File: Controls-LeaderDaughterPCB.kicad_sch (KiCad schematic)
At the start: 30 parts, among them U8 LMC555xM

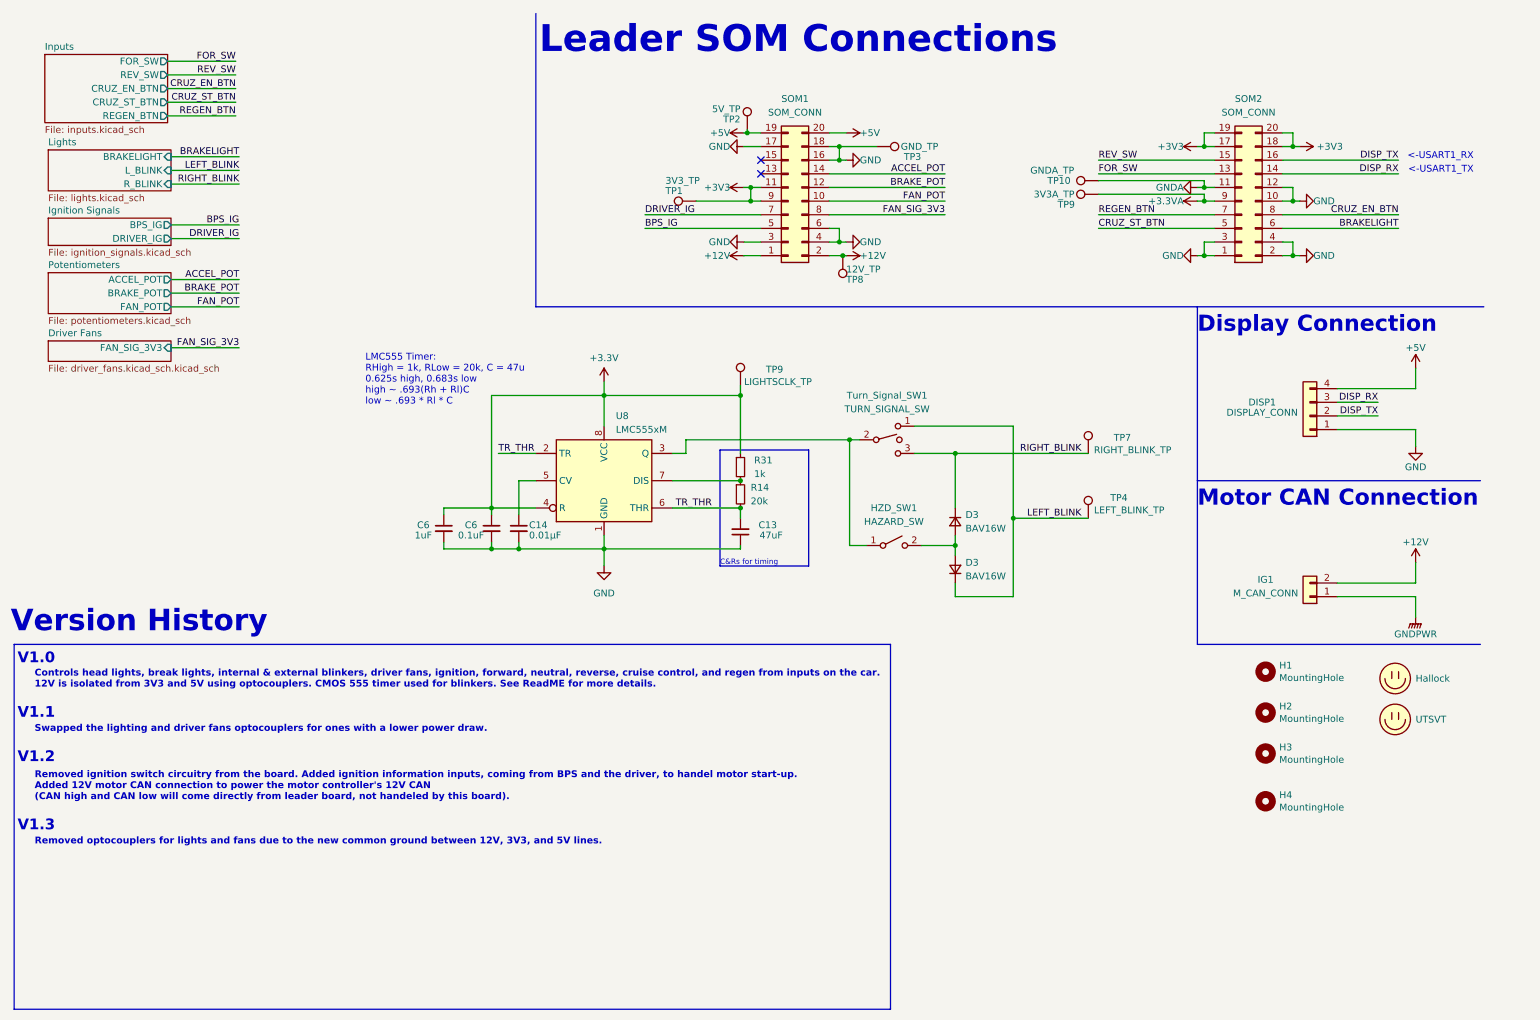
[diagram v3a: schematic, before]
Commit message: Added I2C GPIO expander to reduce GPIO pins from LeaderSOM and replace 555 timer circuit. Adjusted ignition switch signals.
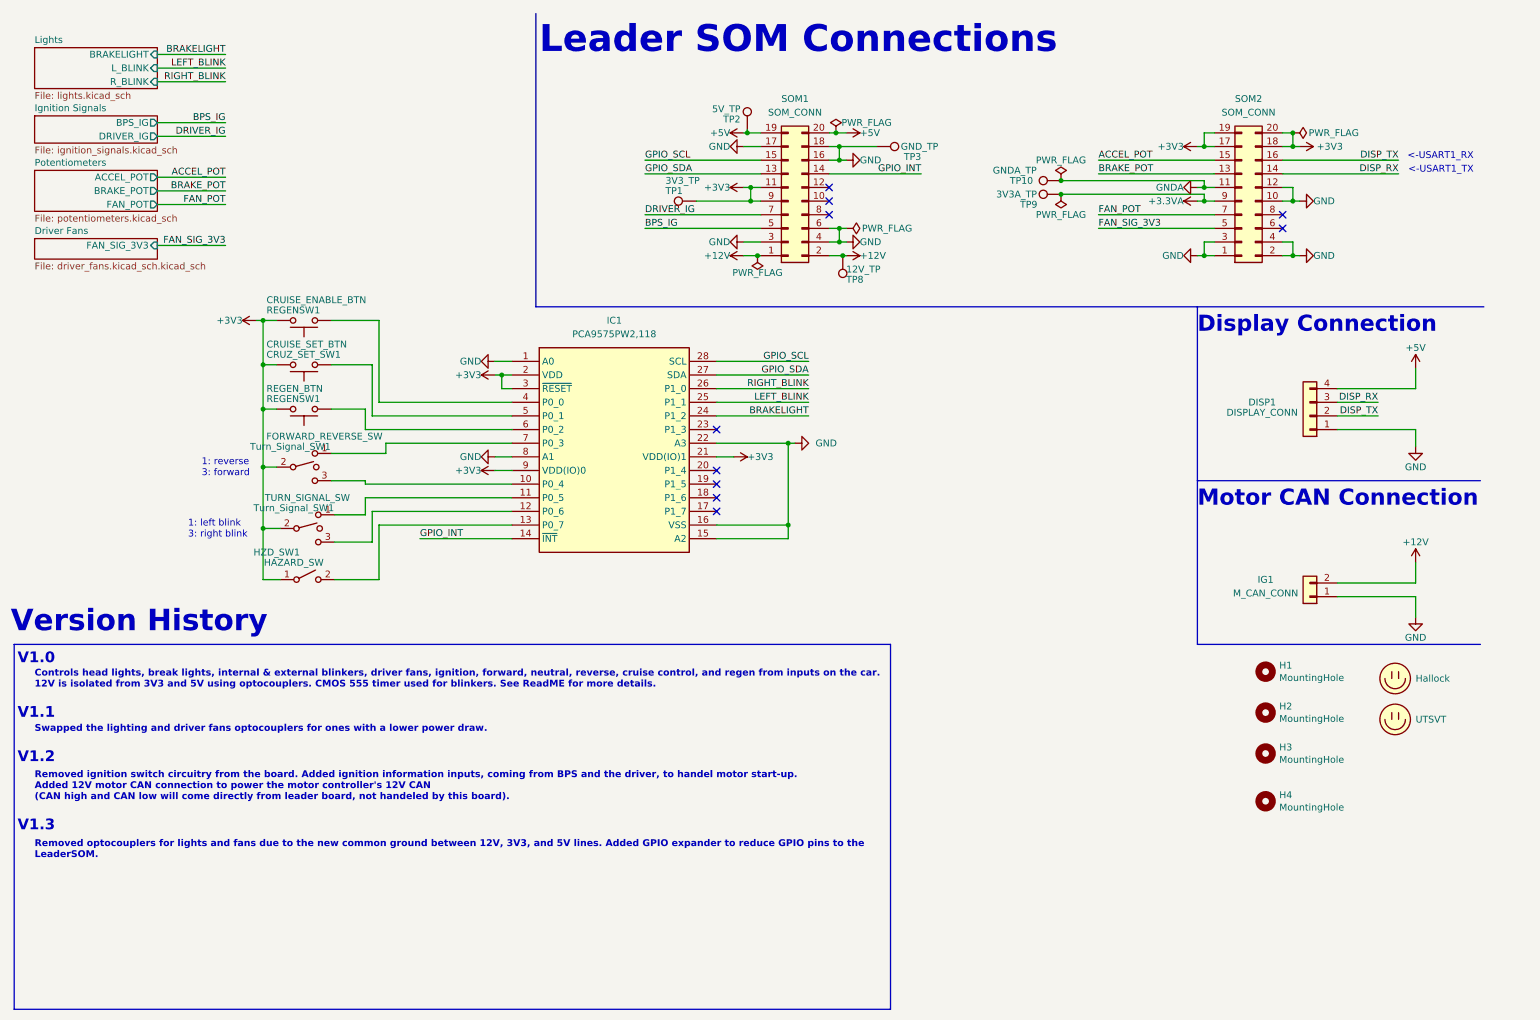
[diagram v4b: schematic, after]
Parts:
- removed C13: 47uF, Capacitor_SMD:C_0805_2012Metric, symbol Device:C_Small
- removed C14: 0.01µF, Capacitor_SMD:C_0805_2012Metric, symbol Device:C_Small
- removed C6: 1uF, Capacitor_SMD:C_0805_2012Metric, symbol Device:C_Small
- removed C6: 0.1uF, Capacitor_SMD:C_0805_2012Metric, symbol Device:C_Small
- removed D3 (x2): BAV16W, Diode_SMD:D_SOD-123, symbol Device:D_Small
- removed R14: 20k, Resistor_SMD:R_0805_2012Metric, symbol Device:R_Small
- removed R31: 1k, Resistor_SMD:R_0805_2012Metric, symbol Device:R_Small
- removed TP4: LEFT_BLINK_TP, TestPoint:TestPoint_Pad_1.5x1.5mm, symbol Connector:TestPoint
- removed TP7: RIGHT_BLINK_TP, TestPoint:TestPoint_Pad_1.5x1.5mm, symbol Connector:TestPoint
- removed TP9: LIGHTSCLK_TP, TestPoint:TestPoint_Pad_1.5x1.5mm, symbol Connector:TestPoint
- removed U8: LMC555xM, Package_SO:SOIC-8_3.9x4.9mm_P1.27mm, symbol Timer:LMC555xM
- added CRUZ_SET_SW1: CRUISE_SET_BTN, Connector_Molex:Molex_Micro-Fit_3.0_43650-0215_1x02_P3.00mm_Vertical, symbol Switch:SW_Push
- added IC1: PCA9575PW2,118, SOP65P640X110-28N, symbol utsvt-chips:PCA9575PW2,118
- added REGENSW1: REGEN_BTN, Connector_Molex:Molex_Micro-Fit_3.0_43650-0215_1x02_P3.00mm_Vertical, symbol Switch:SW_Push
- added REGENSW1: CRUISE_ENABLE_BTN, Connector_Molex:Molex_Micro-Fit_3.0_43650-0215_1x02_P3.00mm_Vertical, symbol Switch:SW_Push
- added Turn_Signal_SW1: FORWARD_REVERSE_SW, Connector_Molex:Molex_Micro-Fit_3.0_43650-0315_1x03_P3.00mm_Vertical, symbol Switch:SW_SPDT_MSM
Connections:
- net CRUZ_ST_BTN is gone; now on net FAN_SIG_3V3: SOM2.5 (Pin_5)
- net FOR_SW is gone; now on net BRAKE_POT: SOM2.13 (Pin_13)
- net GNDPWR is gone; now on net GND: IG1.1 (Pin_1)
- net REGEN_BTN is gone; now on net FAN_POT: SOM2.7 (Pin_7)
- net REV_SW is gone; now on net ACCEL_POT: SOM2.15 (Pin_15)
- net +3V3: now also HZD_SW1.1 (A), Turn_Signal_SW1.2, CRUZ_SET_SW1.2, IC1.2 (VDD), IC1.21 (VDD(IO)1), IC1.3 (~{RESET}), IC1.9 (VDD(IO)0), REGENSW1.2, REGENSW1.2, Turn_Signal_SW1.2
- net ACCEL_POT: no longer SOM1.14 (Pin_14)
- net BRAKELIGHT: now also IC1.24 (P1_2); no longer SOM2.6 (Pin_6)
- net BRAKE_POT: no longer SOM1.12 (Pin_12)
- net FAN_POT: no longer SOM1.10 (Pin_10)
- net FAN_SIG_3V3: no longer SOM1.8 (Pin_8)
- net GND: now also IC1.1 (A0), IC1.15 (A2), IC1.16 (VSS), IC1.22 (A3), IC1.8 (A1)
- net LEFT_BLINK: now also IC1.25 (P1_1); no longer Turn_Signal_SW1.1
- net RIGHT_BLINK: now also IC1.26 (P1_0); no longer Turn_Signal_SW1.3
- net at HZD_SW1.2 (B): now also IC1.13 (P0_7)
- net GPIO_SDA: now reaches SOM1.13 (Pin_13)
- net GPIO_SDA: now also IC1.27 (SDA)
- net GPIO_SCL: now reaches SOM1.15 (Pin_15)
- net GPIO_SCL: now also IC1.28 (SCL)
- net CRUZ_EN_BTN: no longer names the net of SOM2.8 (Pin_8)
- new net: IC1.6 (P0_2), REGENSW1.1
- new net: IC1.7 (P0_3), Turn_Signal_SW1.1
- new net: IC1.10 (P0_4), Turn_Signal_SW1.3
- new net: IC1.11 (P0_5), Turn_Signal_SW1.1
- new net: IC1.12 (P0_6), Turn_Signal_SW1.3
- new net: IC1.4 (P0_0), REGENSW1.1
- new net: CRUZ_SET_SW1.1, IC1.5 (P0_1)
- new net GPIO_INT: IC1.14 (~{INT}), SOM1.14 (Pin_14)
- no-connect marks 2 -> 10
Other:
- removed sheet Inputs
- note added: "1: left blink 3: right blink"
- note added: "1: reverse 3: forward"
- note added: "Removed optocouplers for lights and fans due to the new common ground between 12V, 3V3, and 5V lines. Added GPIO expander to reduce GPIO pins to the LeaderSOM."
- note removed: "C&Rs for timing"
- note removed: "LMC555 Timer: RHigh = 1k, RLow = 20k, C = 47u 0.625s high, 0.683s low high ~ .693(Rh + Rl)C low ~ .693 * Rl * C"
- note removed: "Removed optocouplers for lights and fans due to the new common ground between 12V, 3V3, and 5V lines."
- moved on the sheet: HZD_SW1, TP10, TP9, Turn_Signal_SW1

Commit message: Added debouncing, bypass caps, pull up and down resistors, and current limiting resistors. Removed some TPs.
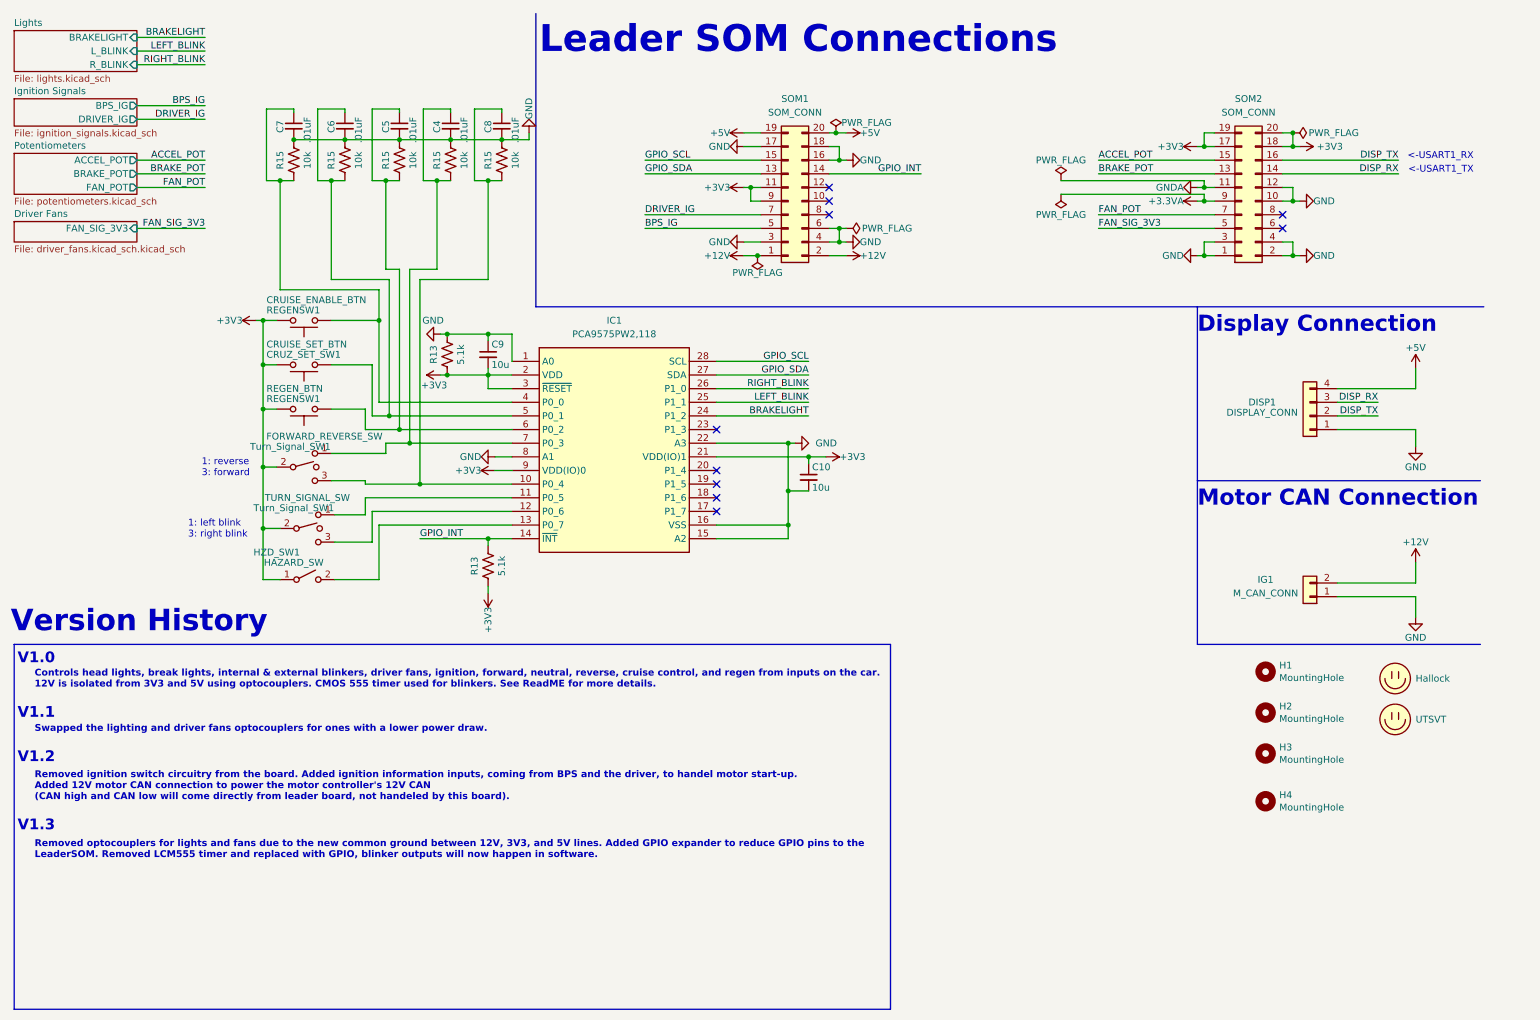
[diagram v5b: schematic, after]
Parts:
- removed TP1: 3V3_TP, TestPoint:TestPoint_Pad_1.5x1.5mm, symbol Connector:TestPoint
- removed TP10: GNDA_TP, TestPoint:TestPoint_Pad_1.5x1.5mm, symbol Connector:TestPoint
- removed TP2: 5V_TP, TestPoint:TestPoint_Pad_1.5x1.5mm, symbol Connector:TestPoint
- removed TP3: GND_TP, TestPoint:TestPoint_Pad_1.5x1.5mm, symbol Connector:TestPoint
- removed TP8: 12V_TP, TestPoint:TestPoint_Pad_1.5x1.5mm, symbol Connector:TestPoint
- removed TP9: 3V3A_TP, TestPoint:TestPoint_Pad_1.5x1.5mm, symbol Connector:TestPoint
- added C10, C9: 10u, symbol Device:C_Small
- added C4, C5, C6, C7, C8: .01uF, symbol Device:C_Small
- added R13 (x2): 5.1k, Resistor_SMD:R_0805_2012Metric, symbol Device:R_US
- added R15 (x5): 10k, Resistor_SMD:R_0805_2012Metric, symbol Device:R_US
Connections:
- net +3V3: now also C10.1, C9.2, R13.2, R13.2
- net GND: now also C10.2, C4.2, C5.2, C6.2, C7.2, C8.2, C9.1, R13.1, R15.1, R15.1, R15.1, R15.1, R15.1
- net GPIO_INT: now also R13.1
- net at IC1.6 (P0_2), REGENSW1.1: now also C5.1, R15.2
- net at IC1.7 (P0_3), Turn_Signal_SW1.1: now also C4.1, R15.2
- net at IC1.10 (P0_4), Turn_Signal_SW1.3: now also C8.1, R15.2
- net at IC1.4 (P0_0), REGENSW1.1: now also C7.1, R15.2
- net at CRUZ_SET_SW1.1, IC1.5 (P0_1): now also C6.1, R15.2
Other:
- note added: "Removed optocouplers for lights and fans due to the new common ground between 12V, 3V3, and 5V lines. Added GPIO expander to reduce GPIO pins to the LeaderSOM. Removed LCM555 timer and replaced with GPIO, blinker outputs will now happen in software."
- note removed: "Removed optocouplers for lights and fans due to the new common ground between 12V, 3V3, and 5V lines. Added GPIO expander to reduce GPIO pins to the LeaderSOM."

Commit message: Organized schematic, removed fan MOSFET
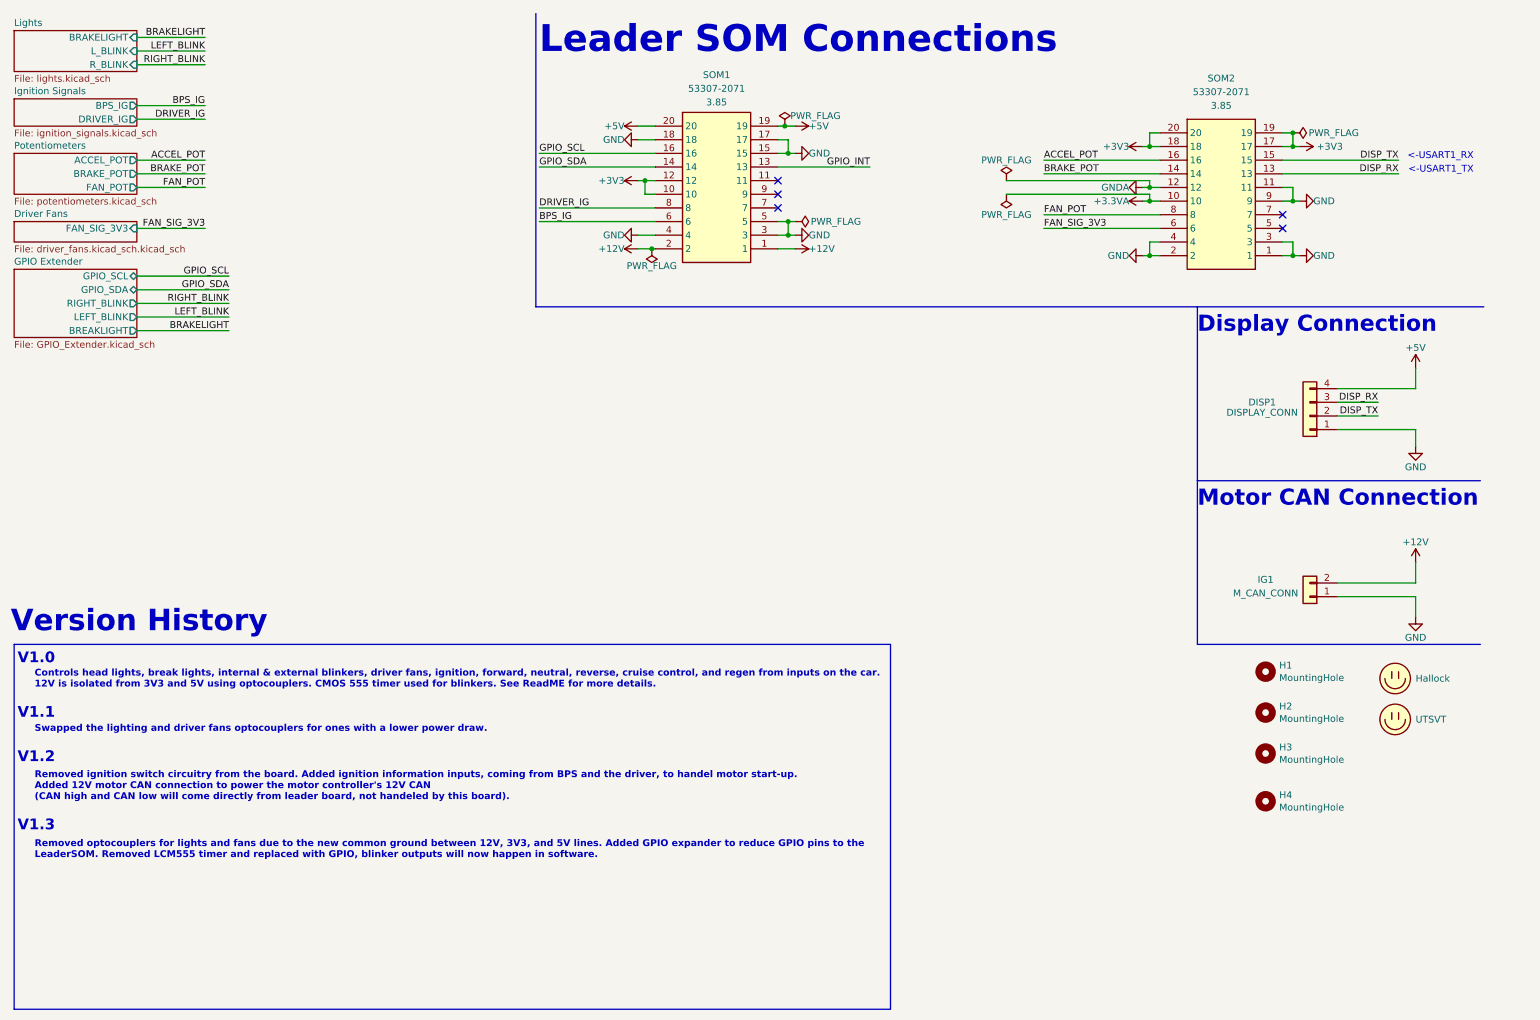
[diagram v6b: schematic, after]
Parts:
- removed C10, C9: 10u, symbol Device:C_Small
- removed C4, C5, C6, C7, C8: .01uF, symbol Device:C_Small
- removed CRUZ_SET_SW1: CRUISE_SET_BTN, Connector_Molex:Molex_Micro-Fit_3.0_43650-0215_1x02_P3.00mm_Vertical, symbol Switch:SW_Push
- removed HZD_SW1: HAZARD_SW, Connector_Molex:Molex_Micro-Fit_3.0_43650-0215_1x02_P3.00mm_Vertical, symbol Switch:SW_SPST
- removed IC1: PCA9575PW2,118, SOP65P640X110-28N, symbol utsvt-chips:PCA9575PW2,118
- removed R13 (x2): 5.1k, Resistor_SMD:R_0805_2012Metric, symbol Device:R_US
- removed R15 (x5): 10k, Resistor_SMD:R_0805_2012Metric, symbol Device:R_US
- removed REGENSW1: REGEN_BTN, Connector_Molex:Molex_Micro-Fit_3.0_43650-0215_1x02_P3.00mm_Vertical, symbol Switch:SW_Push
- removed REGENSW1: CRUISE_ENABLE_BTN, Connector_Molex:Molex_Micro-Fit_3.0_43650-0215_1x02_P3.00mm_Vertical, symbol Switch:SW_Push
- removed SOM1, SOM2: SOM_CONN, UTSVT_Connectors:Molex_52465-2070, symbol Connector_Generic:Conn_02x10_Odd_Even
- removed Turn_Signal_SW1: FORWARD_REVERSE_SW, Connector_Molex:Molex_Micro-Fit_3.0_43650-0315_1x03_P3.00mm_Vertical, symbol Switch:SW_SPDT_MSM
- removed Turn_Signal_SW1: TURN_SIGNAL_SW, Connector_Molex:Molex_Micro-Fit_3.0_43650-0315_1x03_P3.00mm_Vertical, symbol Switch:SW_SPDT_MSM
- added SOM1, SOM2: ~, UTSVT_Special:PeripheralSOM, symbol utsvt-misc:PeripheralSOM
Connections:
- net +12V: now also SOM1.1, SOM1.2
- net +3.3VA: now also SOM2.10
- net +3V3: now also SOM1.10, SOM1.12, SOM2.17, SOM2.18, SOM2.19, SOM2.20
- net +5V: now also SOM1.19, SOM1.20
- net ACCEL_POT: now also SOM2.16
- net BPS_IG: now also SOM1.6
- net BRAKE_POT: now also SOM2.14
- net DISP_RX: now also SOM2.13
- net DISP_TX: now also SOM2.15
- net DRIVER_IG: now also SOM1.8
- net FAN_POT: now also SOM2.8
- net FAN_SIG_3V3: now also SOM2.6
- net GND: now also SOM1.15, SOM1.17, SOM1.18, SOM1.3, SOM1.4, SOM1.5, SOM2.1, SOM2.11, SOM2.2, SOM2.3, SOM2.4, SOM2.9
- net GNDA: now also SOM2.12
- net GPIO_INT: now also SOM1.13
- net GPIO_SCL: now also SOM1.16
- net GPIO_SDA: now also SOM1.14
- no-connect marks 10 -> 5
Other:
- added sheet GPIO Extender (GPIO_Extender.kicad_sch)
- note removed: "1: left blink 3: right blink"
- note removed: "1: reverse 3: forward"
